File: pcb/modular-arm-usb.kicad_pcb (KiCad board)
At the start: 2 copper layers, 28 parts, among them CON1 ARM-SWD-HEADER, IC1 LPC11U14FBD48, P1 USB, P2 UNFUSED_PWR, P3 BATT, P4 GPIO, P5 BATT, P6 GPIO2, U2 LD1117V33, U3 NRF24L01+

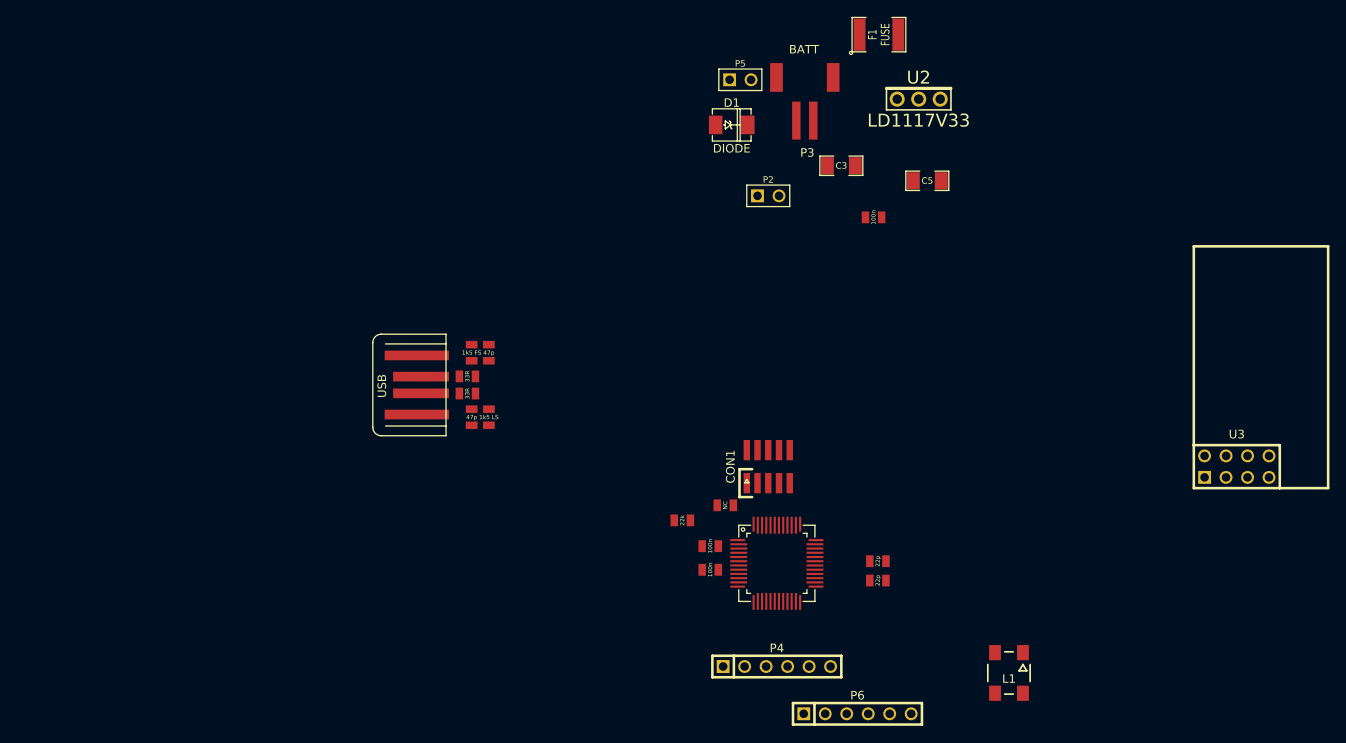
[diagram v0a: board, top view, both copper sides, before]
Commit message: updated kicad to latest version and fixed things that didn't show up properly (text, nrf24l01+ part)
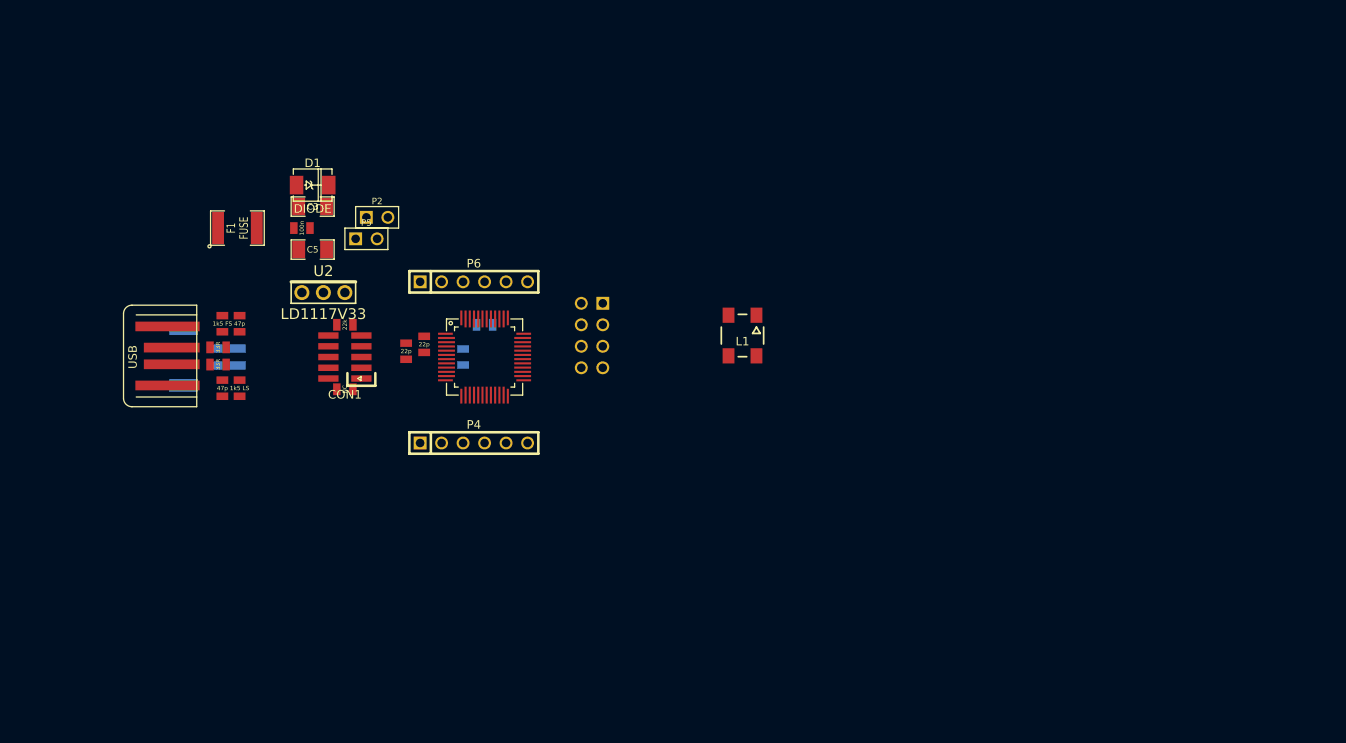
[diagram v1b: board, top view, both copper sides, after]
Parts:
- C1, C2, P3: moved to B.Cu
- U3: value NRF24L01+ -> nRF24L01+; moved to B.Cu
- moved F1 79.2 mm to (99.1, 74.9)
- moved U3 77.8 mm to (141.0, 87.6), turned to 270 degrees
- moved U2 74.0 mm to (106.7, 82.5)
- moved P3 73.8 mm to (97.8, 90.2), turned to 270 degrees
- moved C5 73.1 mm to (108.0, 77.5)
- moved P6 68.3 mm to (127.0, 81.3)
- moved C4 67.6 mm to (106.7, 74.9)
- moved C3 62.7 mm to (108.0, 72.4)
- moved C7 62.0 mm to (119.0, 89.5), turned to 270 degrees
- moved C6 59.4 mm to (121.1, 88.7), turned to 270 degrees
- moved CON1 51.7 mm to (111.8, 90.2), turned to 90 degrees
- moved L1 50.8 mm to (158.8, 87.6)
- moved D1 50.0 mm to (108.0, 69.8)
- moved P5 48.0 mm to (114.3, 76.2)
- moved R1 47.0 mm to (111.8, 94.0)
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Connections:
- CON1 pad 7: (no net) -> Net-(CON1-Pad7)
- CON1 pad 8: (no net) -> Net-(CON1-Pad8)
- IC1 pad 1: (no net) -> Net-(IC1-Pad1)
- IC1 pad 14: (no net) -> LPC_USB_VBUS
- IC1 pad 2: (no net) -> Net-(IC1-Pad2)
- IC1 pad 21: (no net) -> Net-(IC1-Pad21)
- IC1 pad 22: (no net) -> LPC_nUSB_CONNECT
- IC1 pad 30: (no net) -> /lpc-mcu/AD6
- IC1 pad 35: (no net) -> /lpc-mcu/AD3
- IC1 pad 36: (no net) -> Net-(IC1-Pad36)
- IC1 pad 37: (no net) -> Net-(IC1-Pad37)
- IC1 pad 38: (no net) -> Net-(IC1-Pad38)
- IC1 pad 4: (no net) -> /lpc-mcu/CLKOUT
- IC1 pad 40: (no net) -> /lpc-mcu/AD5
- IC1 pad 42: (no net) -> /lpc-mcu/AD7
- IC1 pad 43: (no net) -> Net-(IC1-Pad43)
- IC1 pad 45: (no net) -> Net-(IC1-Pad45)
- IC1 pad 46: (no net) -> Net-(IC1-Pad46)
- IC1 pad 47: (no net) -> Net-(IC1-Pad47)
- IC1 pad 48: (no net) -> Net-(IC1-Pad48)
- IC1 pad 9: (no net) -> Net-(IC1-Pad9)
- L1 pad 2: (no net) -> Net-(L1-Pad2)

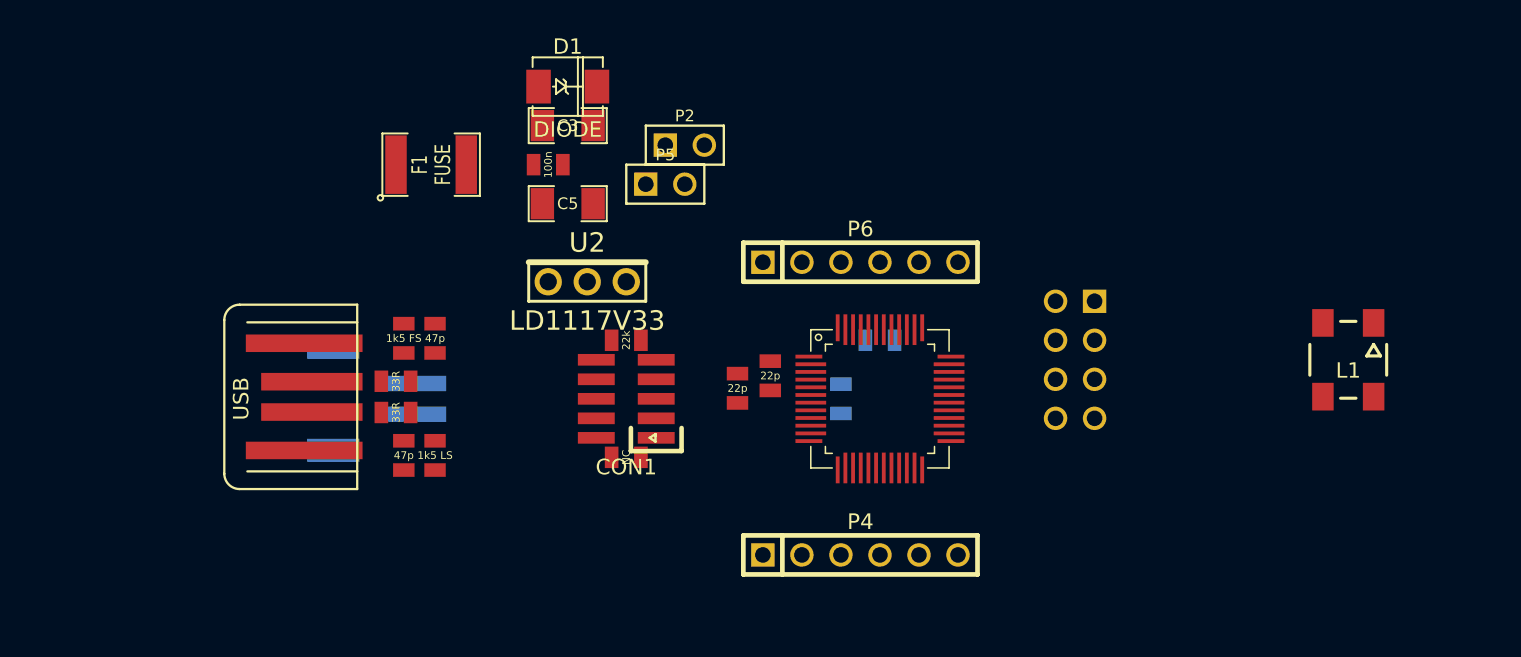
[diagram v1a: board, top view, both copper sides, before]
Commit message: Upgraded all modules to new kicad_mod/pretty format.  Added MCP1700T-3302 regulator and cleaned up power circuit.  Getting closer to final power/USB placement.
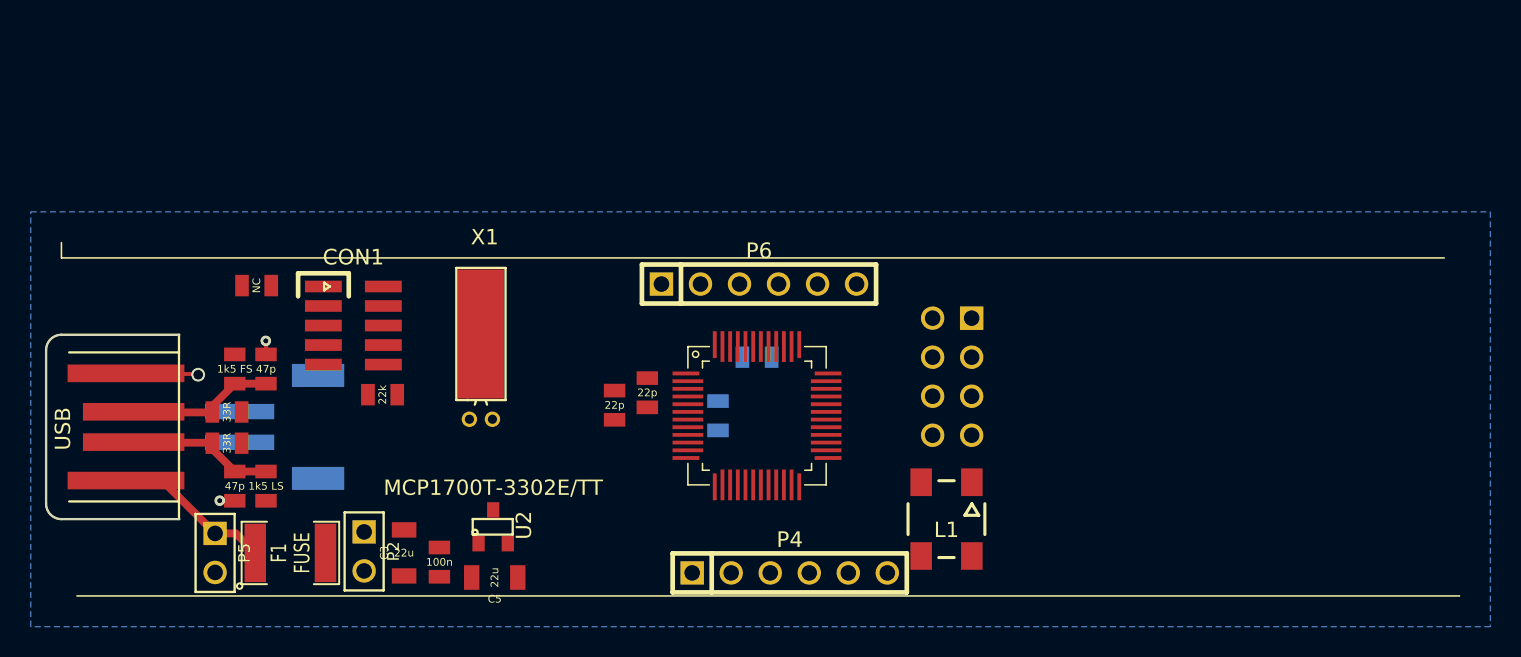
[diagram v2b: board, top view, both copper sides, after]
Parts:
- removed D1: DIODE, DO-214AC(SMA)
- added X1: CRYSTAL, myelin:Crystal_Round_Horizontal_3mm_can_pad, F.Cu at (102.3, 91.5)
- C3, C5: footprint SM1206 -> myelin:SM1206_nosilkscreen
- C4: footprint SM0805_NOSILKSCREEN -> myelin:SM0805_NOSILKSCREEN
- U2: value LD1117V33 -> MCP1700T-3302E/TT; footprint LD1117V33 -> SMD_Packages:SOT-23
- moved P5 37.9 mm to (85.0, 100.2), turned to 270 degrees
- moved P2 33.7 mm to (94.7, 100.1), turned to 270 degrees
- moved C3 29.8 mm to (97.3, 100.2), turned to 270 degrees
- moved L1 28.1 mm to (132.6, 98.0)
- moved F1 26.9 mm to (89.9, 100.2)
- moved C4 26.8 mm to (99.6, 100.8), turned to 270 degrees
- moved R1 26.5 mm to (87.7, 82.8)
- moved C5 24.8 mm to (103.2, 101.8), turned to 180 degrees
- moved CON1 18.4 mm to (94.0, 85.4), turned to 270 degrees
- moved U2 16.3 mm to (103.1, 98.5)
- moved R2 16.3 mm to (95.9, 89.9)
- moved P1 11.8 mm to (74.0, 92.0)
- moved P3 11.3 mm to (86.6, 92.0), turned to 90 degrees
- moved C8 11.2 mm to (86.3, 95.9)
- moved C9 11.2 mm to (88.3, 88.2)
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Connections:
- P3 pad 2: Net-(D1-Pad1) -> VUSB
- P5 pad 1: Net-(D1-Pad1) -> VUSB
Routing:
- net VUSB: track 0.00 -> 9.75 mm
- net /usb/DP: track 0.00 -> 9.01 mm
- net /usb/DM: track 0.00 -> 9.01 mm
- net GND: track 0.00 -> 5.99 mm, vias 0 -> 3
- added copper zone on B.Cu, net GND
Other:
- board outline added: 8.7 x 12 mm

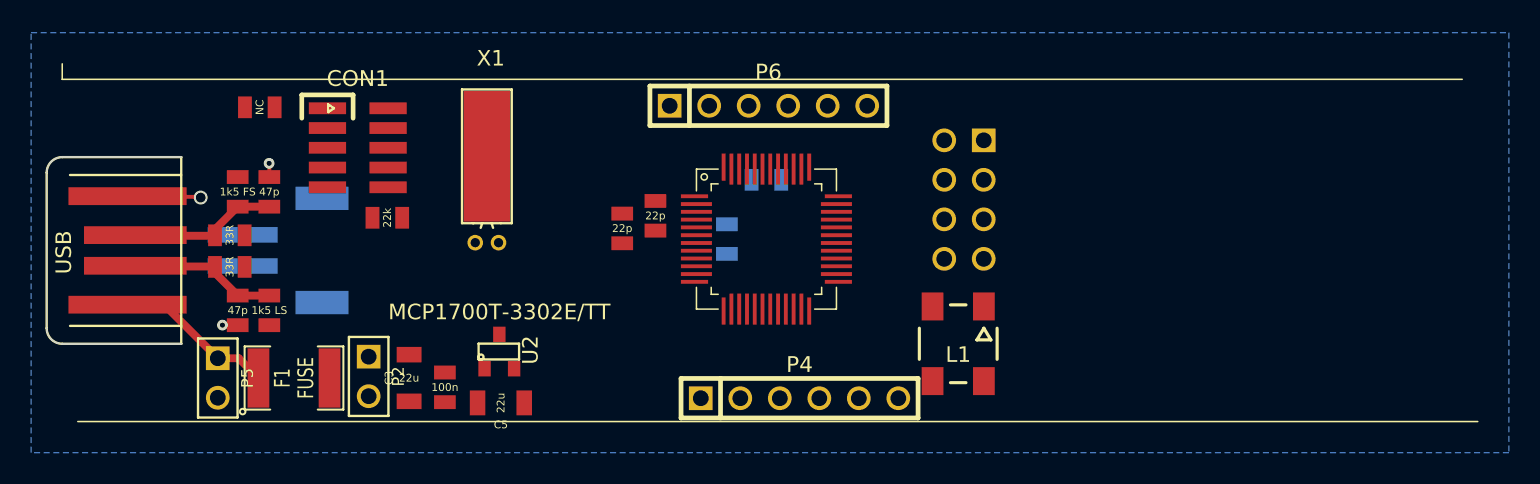
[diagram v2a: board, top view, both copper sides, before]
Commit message: moved things around on the pcb a bit, made it more compact
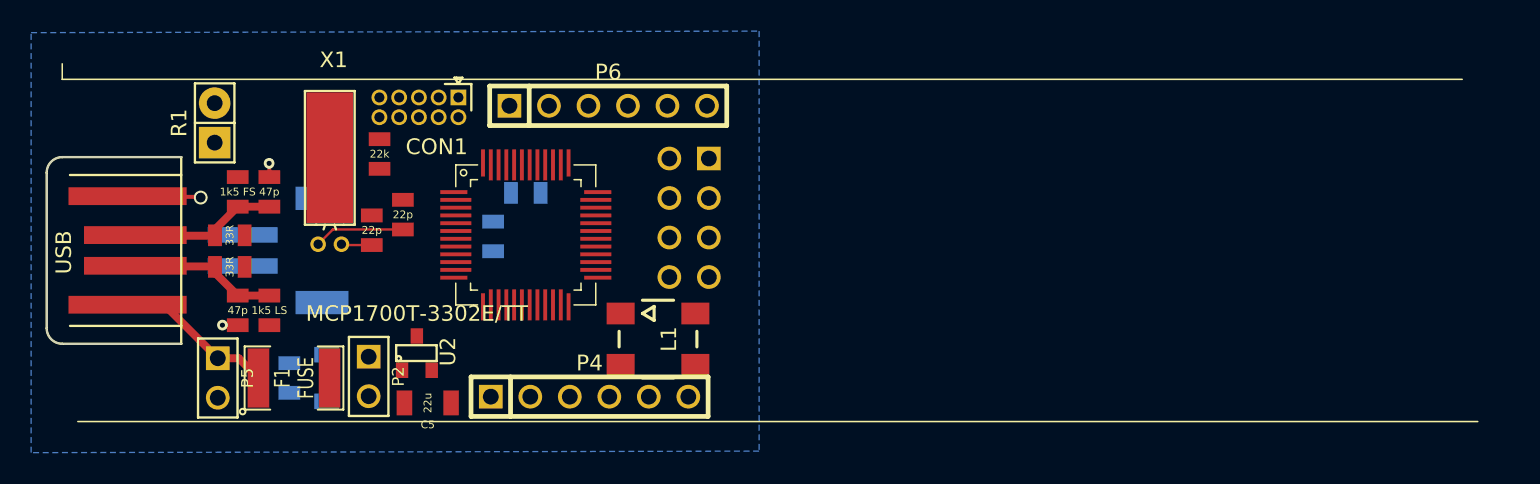
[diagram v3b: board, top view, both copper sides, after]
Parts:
- C3, C4: moved to B.Cu
- CON1: footprint pin_array_5x2_50mil_smd -> myelin:pin_array_5x2_50mil
- R1: footprint SM0805_NOSILKSCREEN -> Pin_Headers:Pin_Header_Straight_1x02
- X1: value CRYSTAL -> 16M xtal
- moved L1 19.3 mm to (113.3, 97.7), turned to 90 degrees
- moved U3 17.7 mm to (115.3, 89.9)
- moved C6 16.2 mm to (96.9, 89.7)
- moved C7 16.1 mm to (94.9, 90.7)
- moved C2 15.5 mm to (104.8, 88.3)
- moved IC1 15.5 mm to (104.8, 91.0)
- moved C1 15.0 mm to (102.7, 91.1)
- moved P4 13.5 mm to (108.9, 101.4)
- moved P6 10.3 mm to (110.1, 82.7)
- moved X1 10.1 mm to (92.2, 91.6)
- moved C4 10.0 mm to (89.6, 100.2)
- moved CON1 5.81 mm to (99.2, 82.8), turned to 180 degrees
- moved U2 5.30 mm to (97.8, 98.6)
- moved C3 5.30 mm to (92.0, 100.2)
- moved C5 4.70 mm to (98.5, 101.8)
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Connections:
- X1 pad 1: /lpc-mcu/XTALOUT -> /lpc-mcu/XTALIN
- X1 pad 2: /lpc-mcu/XTALIN -> /lpc-mcu/XTALOUT
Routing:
- net /lpc-mcu/XTALIN: track 0.00 -> 5.84 mm
- net /lpc-mcu/XTALOUT: track 0.00 -> 1.97 mm

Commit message: pcb work from last night
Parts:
- removed R1: NC, Pin_Headers:Pin_Header_Straight_1x02
- added JP1: NC, myelin:PIN_ARRAY_2X1, F.Cu at (96.2, 82.5)
- added SW1: SW_SPDT, myelin:PIN_ARRAY_3X1, F.Cu at (90.4, 101.0)
- added SW2: SW_PUSH_ALT, OMRON-PUSH-BUTTON-B3SN-3112P:OMRON-PUSH-BUTTON-B3SN-3112P, F.Cu at (94.1, 92.2)
- C1, C2, C6, C7, C8, C9, R3, R4, R5, R6: footprint SM0805_NOSILKSCREEN -> myelin:SM0805_NOSILKSCREEN
- C3: value 22u -> 10u; footprint myelin:SM1206_nosilkscreen -> myelin:SM0805_NOSILKSCREEN
- C5: value 22u -> 10u; footprint myelin:SM1206_nosilkscreen -> myelin:SM0805_NOSILKSCREEN; moved to B.Cu
- CON1: value ARM-SWD-HEADER -> SWD
- F1: footprint SM1812 -> SMD_Packages:SMD-1812
- IC1: footprint NXP_LQFP48_BY_HAND -> myelin:NXP_LQFP48_BY_HAND
- L1: footprint WS2812B_PP -> myelin:WS2812B_PP
- P1: footprint USB_A_PCB -> myelin:USB_A_PCB
- P2: value UNFUSED_PWR -> LED; footprint PIN_ARRAY_2X1 -> Pin_Headers:Pin_Header_Straight_1x01; moved to B.Cu
- P3: footprint S2B-PH-SM4-TB(LF)(SN) -> myelin:S2B-PH-SM4-TB(LF)(SN)
- P4, P6: footprint PIN_ARRAY-6X1 -> myelin:PIN_ARRAY_6X1
- P5: value BATT -> gnd; footprint PIN_ARRAY_2X1 -> Pin_Headers:Pin_Header_Straight_1x01
- R2: footprint SM0805_NOSILKSCREEN -> myelin:SM0805_NOSILKSCREEN; moved to B.Cu
- U2: value MCP1700T-3302E/TT -> MCP1700T; footprint SMD_Packages:SOT-23 -> Housings_SOT-89:SOT89-3_Housing
- U3: footprint NRF24L01_MODULE -> myelin:NRF24L01_MODULE
- moved P2 31.0 mm to (122.3, 85.9), turned to 0 degrees
- moved R2 15.7 mm to (109.8, 92.0)
- moved L1 15.0 mm to (121.2, 84.9), turned to 0 degrees
- moved C4 11.1 mm to (100.7, 100.3), turned to 90 degrees
- moved C3 10.7 mm to (102.7, 100.3), turned to 90 degrees
- moved C7 9.19 mm to (103.0, 95.0), turned to 90 degrees
- moved X1 8.74 mm to (100.1, 95.4)
- moved P5 8.49 mm to (93.3, 98.3), turned to 0 degrees
- moved CON1 8.20 mm to (91.0, 83.0)
- moved F1 8.10 mm to (98.0, 100.5)
- moved U3 7.68 mm to (121.3, 94.7), turned to 90 degrees
- moved C5 7.23 mm to (105.5, 100.2), turned to 90 degrees
- moved P4 7.20 mm to (116.1, 101.3), turned to 180 degrees
- moved U2 7.05 mm to (104.6, 100.5), turned to 270 degrees
- moved C6 6.37 mm to (103.0, 91.5)
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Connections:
- F1 pad 1: VUSB -> /power/VIN
- IC1 pad 1: Net-(IC1-Pad1) -> /lpc-mcu/BUTTON
- IC1 pad 23: /lpc-mcu/LED_INPUT -> Net-(IC1-Pad23)
- IC1 pad 36: Net-(IC1-Pad36) -> /lpc-mcu/LED_INPUT
- P2 pad 1: Net-(C3-Pad1) -> Net-(L1-Pad2)
- P3 pad 2: VUSB -> /power/VBATT
- P4 pad 3: /lpc-mcu/SCL -> /lpc-mcu/SSEL1
- P4 pad 4: /lpc-mcu/SDA -> /lpc-mcu/MISO1
- P4 pad 5: /lpc-mcu/RXD -> /lpc-mcu/MOSI1
- P4 pad 6: /lpc-mcu/TXD -> /lpc-mcu/SCK1
- P5 pad 1: VUSB -> GND
- P6 pad 1: /lpc-mcu/AD0 -> /lpc-mcu/SDA
- P6 pad 2: /lpc-mcu/AD1 -> /lpc-mcu/SCL
- P6 pad 3: /lpc-mcu/SSEL1 -> /lpc-mcu/RXD
- P6 pad 4: /lpc-mcu/MISO1 -> /lpc-mcu/TXD
- P6 pad 5: /lpc-mcu/MOSI1 -> /lpc-mcu/AD0
- P6 pad 6: /lpc-mcu/SCK1 -> /lpc-mcu/AD1
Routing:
- net GND: track 5.99 -> 171.6 mm, vias 3 -> 14
- net 3V3: track 0.00 -> 104.0 mm, vias 0 -> 9
- net LPC_USB_DP: track 0.00 -> 29.7 mm
- net /lpc-mcu/SWO: track 0.00 -> 28.5 mm, vias 0 -> 1
- net /lpc-mcu/SWCLK: track 0.00 -> 28.2 mm
- net LPC_USB_DM: track 0.00 -> 28.1 mm
- net /lpc-mcu/nRESET: track 0.00 -> 27.2 mm, vias 0 -> 3
- net /lpc-mcu/RXD: track 0.00 -> 23.6 mm, vias 0 -> 2
- net /lpc-mcu/SWDIO: track 0.00 -> 22.7 mm
- net /lpc-mcu/TXD: track 0.00 -> 22.5 mm, vias 0 -> 2
- net /lpc-mcu/SDA: track 0.00 -> 21.5 mm, vias 0 -> 1
- net RF24_CSN: track 0.00 -> 20.3 mm, vias 0 -> 2
- net /lpc-mcu/SCL: track 0.00 -> 19.5 mm, vias 0 -> 1
- net /power/VBATT: track 0.00 -> 15.3 mm
- net RF24_IRQ: track 0.00 -> 14.5 mm, vias 0 -> 1
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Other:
- board size 8.7 x 12 mm -> 50 x 22 mm
- board text added: "1"
- board text added: "3v3"
- board text added: "github.com/ myelin/ modular-arm-usb v1 phil pearson & phil lindsay"
- board text added: "sck mosi miso ss"
- board text added: "sda scl rxd txd ad0 ad1"
